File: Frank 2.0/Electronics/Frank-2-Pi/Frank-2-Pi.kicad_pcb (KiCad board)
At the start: 2 copper layers, 11 parts, among them J2 Left motor, J3 Right motor, Q1 DMN6075S, Q2 DMN6075S, U1 adafruit-2448

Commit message: Frank 2.0 electronics WIP.
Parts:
- added C1: 0.1u, Capacitor_SMD:C_0805_2012Metric, B.Cu at (159.4, 107.0)
- added C10: 100u, Capacitor_Tantalum_SMD:CP_EIA-3216-18_Kemet-A_Pad1.58x1.35mm_HandSolder, B.Cu at (169.5, 98.4)
- added C11: 0.1u, Capacitor_SMD:C_0805_2012Metric, B.Cu at (165.7, 111.5)
- added C12: 0.1u, Capacitor_SMD:C_0805_2012Metric, B.Cu at (132.1, 138.4)
- added C3: 0.1u, Capacitor_SMD:C_0805_2012Metric, B.Cu at (170.8, 120.0)
- added C5: 0.1u, Capacitor_SMD:C_0805_2012Metric, B.Cu at (168.3, 120.0)
- added C6: 0.1u, Capacitor_SMD:C_0805_2012Metric, B.Cu at (181.6, 97.8)
- added C7: 0.1u, Capacitor_SMD:C_0805_2012Metric, B.Cu at (118.7, 144.1)
- added C8: 0.1u, Capacitor_SMD:C_0805_2012Metric, B.Cu at (169.5, 112.1)
- added C9: 10u, Capacitor_Tantalum_SMD:CP_EIA-3216-18_Kemet-A_Pad1.58x1.35mm_HandSolder, B.Cu at (169.5, 103.5)
- added J1: left wheel sensor, Connector_PinHeader_2.54mm:PinHeader_1x04_P2.54mm_Vertical, F.Cu at (174.0, 147.3)
- added J10: USB-to-controller, Connector_USB:USB_Micro-B_Wuerth_629105150521, B.Cu at (152.4, 94.6)
- added J11: power-connector, Connector_PinHeader_2.54mm:PinHeader_1x03_P2.54mm_Vertical, F.Cu at (121.3, 91.4)
- added J12: servo 3, Connector_PinHeader_2.54mm:PinHeader_1x03_P2.54mm_Vertical, F.Cu at (111.8, 113.7)
- added J13: servo 2, Connector_PinHeader_2.54mm:PinHeader_1x03_P2.54mm_Vertical, F.Cu at (111.8, 109.2)
- added J14: servo 1, Connector_PinHeader_2.54mm:PinHeader_1x03_P2.54mm_Vertical, F.Cu at (111.8, 104.8)
- added J15: GPIO, Connector_PinHeader_2.54mm:PinHeader_1x05_P2.54mm_Vertical, F.Cu at (111.8, 118.7)
- added J16: data-connector, Connector_PinHeader_2.54mm:PinHeader_1x04_P2.54mm_Vertical, F.Cu at (160.7, 91.4)
- added J4: right wheel sensor, Connector_PinHeader_2.54mm:PinHeader_1x04_P2.54mm_Vertical, F.Cu at (136.5, 147.3)
- added J5: Analogue inputs, Connector_PinHeader_2.54mm:PinHeader_1x03_P2.54mm_Vertical, F.Cu at (181.6, 131.4)
- added J6: LIDAR, Connector_PinHeader_2.54mm:PinHeader_1x04_P2.54mm_Vertical, F.Cu at (112.4, 147.3)
- added J7: Phototransistor, Connector_PinHeader_2.54mm:PinHeader_1x02_P2.54mm_Vertical, F.Cu at (127.0, 147.3)
- added J8: USB-from-battery, Connector_USB:USB_Micro-B_Wuerth_629105150521, B.Cu at (134.0, 94.6)
- added J9: power switch, Connector_PinHeader_2.54mm:PinHeader_1x02_P2.54mm_Vertical, F.Cu at (144.1, 91.4)
- added JP1: l->a2, Jumper:SolderJumper-2_P1.3mm_Open_RoundedPad1.0x1.5mm, B.Cu at (182.9, 118.1)
- added JP2: r->a3, Jumper:SolderJumper-2_P1.3mm_Open_RoundedPad1.0x1.5mm, B.Cu at (182.9, 122.6)
- added R1: 220R, Resistor_SMD:R_0805_2012Metric, B.Cu at (174.0, 143.2)
- added R10: 33K, Resistor_SMD:R_0805_2012Metric, B.Cu at (162.6, 111.8)
- added R11: 15K, Resistor_SMD:R_0805_2012Metric, B.Cu at (172.7, 108.6)
- added R12: 10K, Resistor_SMD:R_0805_2012Metric, B.Cu at (172.7, 112.4)
- added R13: 15K, Resistor_SMD:R_0805_2012Metric, B.Cu at (182.9, 113.7)
- added R2: 220R, Resistor_SMD:R_0805_2012Metric, B.Cu at (136.5, 143.2)
- added R7: 10K, Resistor_SMD:R_0805_2012Metric, B.Cu at (181.6, 143.2)
- added R8: 10K, Resistor_SMD:R_0805_2012Metric, B.Cu at (144.1, 143.2)
- added R9: 6K8, Resistor_SMD:R_0805_2012Metric, B.Cu at (162.6, 107.3)
- added U2: LM2903, Package_SO:Diodes_SO-8EP, B.Cu at (151.1, 108.6)
- added U3: adafruit-1015, reprapltd-kicad:adafruit-1015, F.Cu at (178.4, 108.0)
- added U4: AP1117-33, Package_TO_SOT_SMD:SOT-223-3_TabPin2, B.Cu at (161.9, 101.0)
- added U5: sparkfun-sx1509, reprapltd-kicad:sparkfun-sx1509, F.Cu at (139.7, 131.4)
- C2, C4, Q1, Q2, R3, R4, R5, R6: moved to B.Cu
- moved J2 464.9 mm to (163.2, 147.3), turned to 90 degrees
- moved J3 462.2 mm to (153.0, 147.3), turned to 90 degrees
- moved C4 459.4 mm to (154.3, 144.1)
- moved C2 451.4 mm to (164.5, 144.1)
- moved R5 443.5 mm to (160.7, 129.8), turned to 90 degrees
- moved U1 442.2 mm to (159.4, 133.3), turned to 90 degrees
- moved R6 438.9 mm to (150.5, 129.8), turned to 90 degrees
- moved Q1 431.7 mm to (161.0, 121.0), turned to 270 degrees
- moved R4 430.7 mm to (149.9, 116.5), turned to 90 degrees
- moved Q2 428.9 mm to (150.8, 121.0), turned to 270 degrees
- moved R3 422.5 mm to (160.0, 116.5), turned to 90 degrees
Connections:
- net GPIO16 renamed IO2
- net GPIO6 renamed IO1
- U1 pad 12: GPIO12 -> IO3
- U1 pad 18: GPIO13 -> IO0
- U1 pad 7: Net-(U1-Pad7) -> GND

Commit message: Now with indicator LEDs...
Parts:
- added D1: FLASH, LED_SMD:LED_0805_2012Metric, B.Cu at (115.6, 120.0)
- added D2: 5VLED, LED_SMD:LED_0805_2012Metric, B.Cu at (120.7, 98.4)
- added D3: 3V3LED, LED_SMD:LED_0805_2012Metric, B.Cu at (120.7, 95.9)
- added R14: 220R, Resistor_SMD:R_0805_2012Metric, B.Cu at (120.0, 118.1)
- added R15: 220R, Resistor_SMD:R_0805_2012Metric, B.Cu at (126.4, 95.2)
- added R16: 220R, Resistor_SMD:R_0805_2012Metric, B.Cu at (123.8, 95.2)
- J15: footprint Connector_PinHeader_2.54mm:PinHeader_1x05_P2.54mm_Vertical -> Connector_PinHeader_2.54mm:PinHeader_1x04_P2.54mm_Vertical
- moved J15 4.44 mm to (111.8, 123.2)
- moved U5 1.91 mm to (139.7, 133.3)
- moved C12 1.27 mm to (132.1, 139.7)
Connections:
- J15 pad 4: Net-(J15-Pad4) -> GND
- U5 pad 6: Net-(J15-Pad1) -> Net-(D1-Pad1)
- U5 pad 7: Net-(J15-Pad2) -> Net-(J15-Pad1)
- U5 pad 8: Net-(J15-Pad3) -> Net-(J15-Pad2)
- U5 pad 9: Net-(J15-Pad4) -> Net-(J15-Pad3)
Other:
- board text added: "LEDs are underneath..."

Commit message: Electronics WIP
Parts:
- added C13: 0.1u, Capacitor_SMD:C_0805_2012Metric, B.Cu at (155.6, 95.9)
- added C14: 0.1u, Capacitor_SMD:C_0805_2012Metric, B.Cu at (174.6, 98.4)
- D1, D2, D3: footprint LED_SMD:LED_0805_2012Metric -> LED_THT:LED_D3.0mm; moved to F.Cu
- moved D3 50.0 mm to (170.2, 102.9), turned to 270 degrees
- moved R16 47.8 mm to (169.5, 109.2), turned to 270 degrees
- moved D2 43.4 mm to (163.8, 102.9), turned to 270 degrees
- moved R15 43.0 mm to (167.0, 109.2), turned to 270 degrees
- moved C1 39.5 mm to (170.8, 144.8)
- moved J11 38.7 mm to (160.0, 91.4)
- moved U2 36.3 mm to (148.6, 144.8)
- moved C8 34.9 mm to (181.0, 145.1)
- moved R9 34.9 mm to (174.0, 140.3)
- moved R10 34.9 mm to (174.0, 144.8)
- moved R11 34.9 mm to (184.2, 141.6)
- moved R12 34.9 mm to (184.2, 145.4)
- moved C11 34.9 mm to (177.2, 144.5)
- moved J16 16.5 mm to (177.2, 91.4), turned to 270 degrees
- moved C9 12.9 mm to (158.8, 96.5), turned to 270 degrees
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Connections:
- R3 pad 2: IO2 -> IO1
- R4 pad 2: IO1 -> IO2
- U1 pad 12: IO3 -> IO0
- U1 pad 14: IO2 -> IO1
- U1 pad 16: IO1 -> IO2
- U1 pad 18: IO0 -> IO3
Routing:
- net +5V: track 0.00 -> 57.4 mm, vias 0 -> 2
- net Net-(J10-Pad2): track 0.00 -> 32.5 mm
- net Net-(J8-Pad1): track 0.00 -> 15.8 mm
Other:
- board text removed: "LEDs are underneath..."

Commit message: PCB WIP
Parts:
- added H1: MountingHole, MountingHole:MountingHole_3.2mm_M3, F.Cu at (107.0, 95.0)
- added H2: MountingHole, MountingHole:MountingHole_3.2mm_M3, F.Cu at (107.0, 155.0)
- added H3: MountingHole, MountingHole:MountingHole_3.2mm_M3, F.Cu at (170.0, 95.0)
- added H4: MountingHole, MountingHole:MountingHole_3.2mm_M3, F.Cu at (170.0, 155.0)
- U2: footprint Package_SO:Diodes_SO-8EP -> reprapltd-kicad:Diodes_SO-8EP
- moved J6 65.2 mm to (172.1, 115.7), turned to 0 degrees
- moved C7 52.3 mm to (172.0, 126.7)
- moved R12 50.1 mm to (145.5, 113.5), turned to 180 degrees
- moved C8 49.6 mm to (145.5, 110.4), turned to 180 degrees
- moved J7 45.7 mm to (172.0, 131.6), turned to 0 degrees
- moved R11 44.7 mm to (149.4, 113.5), turned to 180 degrees
- moved C6 42.7 mm to (140.7, 110.0), turned to 0 degrees
- moved C14 41.2 mm to (134.6, 108.2)
- moved C9 41.0 mm to (118.6, 104.8)
- moved U4 41.0 mm to (125.0, 105.4)
- moved C10 41.0 mm to (131.3, 106.7)
- moved J9 37.8 mm to (105.4, 104.4), turned to 180 degrees
- moved J16 33.0 mm to (144.1, 90.8), turned to 90 degrees
- moved U3 27.3 mm to (151.1, 107.3), turned to 90 degrees
- moved C1 27.2 mm to (148.3, 129.5), turned to 0 degrees
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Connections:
- J1 pad 2: IO4 -> IO0
- J4 pad 2: IO6 -> IO2
- R3 pad 2: IO1 -> IO5
- R4 pad 2: IO2 -> IO6
- U1 pad 12: IO0 -> IO4
- U1 pad 14: IO1 -> IO5
- U1 pad 16: IO2 -> IO6
- U1 pad 18: IO3 -> IO7
- U2 pad 1: IO5 -> IO1
- U2 pad 7: IO7 -> IO3
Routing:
- net +3V3: track 0.00 -> 272.3 mm, vias 0 -> 2
- net SCL: track 0.00 -> 81.7 mm
- net SDA: track 0.00 -> 78.7 mm
- net +5V: track 57.4 -> 120.8 mm, vias 2 -> 0
- net INTERRUPT: track 0.00 -> 63.1 mm, vias 0 -> 1
- net IO8: track 0.00 -> 42.8 mm, vias 0 -> 1
- net Net-(J7-Pad2): track 0.00 -> 38.3 mm, vias 0 -> 1
- net Net-(C2-Pad2): track 0.00 -> 35.9 mm
- net IO5: track 0.00 -> 35.3 mm
- net Net-(C2-Pad1): track 0.00 -> 35.2 mm
- net IO0: track 0.00 -> 35.2 mm, vias 0 -> 1
- net IO2: track 0.00 -> 34.7 mm
- net Net-(J10-Pad2): track 32.5 -> 0.02 mm
- net Net-(C4-Pad2): track 0.00 -> 31.5 mm
- net Net-(C4-Pad1): track 0.00 -> 31.3 mm
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- added copper zone on B.Cu, net GND
- added copper zone on F.Cu, net GND

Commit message: PCB WIP
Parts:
- moved JP2 59.7 mm to (133.3, 155.2), turned to 0 degrees
- moved JP1 52.5 mm to (148.2, 154.8)
- moved C2 17.5 mm to (161.4, 154.9)
- moved C4 17.5 mm to (154.7, 154.9)
- moved J2 17.5 mm to (160.4, 158.1)
- moved J3 17.5 mm to (153.4, 158.1)
- moved R1 14.0 mm to (137.2, 153.9)
- moved R7 14.0 mm to (144.8, 153.9)
- moved J1 14.0 mm to (137.2, 158.1)
- moved U2 5.14 mm to (147.8, 132.1)
- moved C1 4.32 mm to (150.4, 125.7)
- moved R6 1.77 mm to (145.8, 125.2), turned to 180 degrees
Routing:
- net Net-(J5-Pad3): track 13.9 -> 116.7 mm
- net Net-(J5-Pad2): track 19.8 -> 83.7 mm
- net INTERRUPT: track 63.1 -> 111.9 mm, vias 1 -> 3
- net Net-(J1-Pad4): track 2.57 -> 48.1 mm, vias 0 -> 2
- net SCL: track 81.7 -> 119.1 mm
- net SDA: track 78.7 -> 105.7 mm
- net GND: track 5.21 -> 31.6 mm, vias 0 -> 3
- net Net-(J4-Pad4): track 21.5 -> 47.9 mm, vias 0 -> 2
- net +5V: track 120.8 -> 142.8 mm, vias 0 -> 2
- net Net-(C11-Pad1): track 5.45 -> 19.2 mm
- net IO4: track 28.8 -> 40.5 mm
- net +3V3: track 272.3 -> 283.6 mm
- net IO3: track 13.1 -> 23.6 mm
- net Net-(C2-Pad1): track 35.2 -> 24.7 mm
- net Net-(C2-Pad2): track 35.9 -> 26.5 mm
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
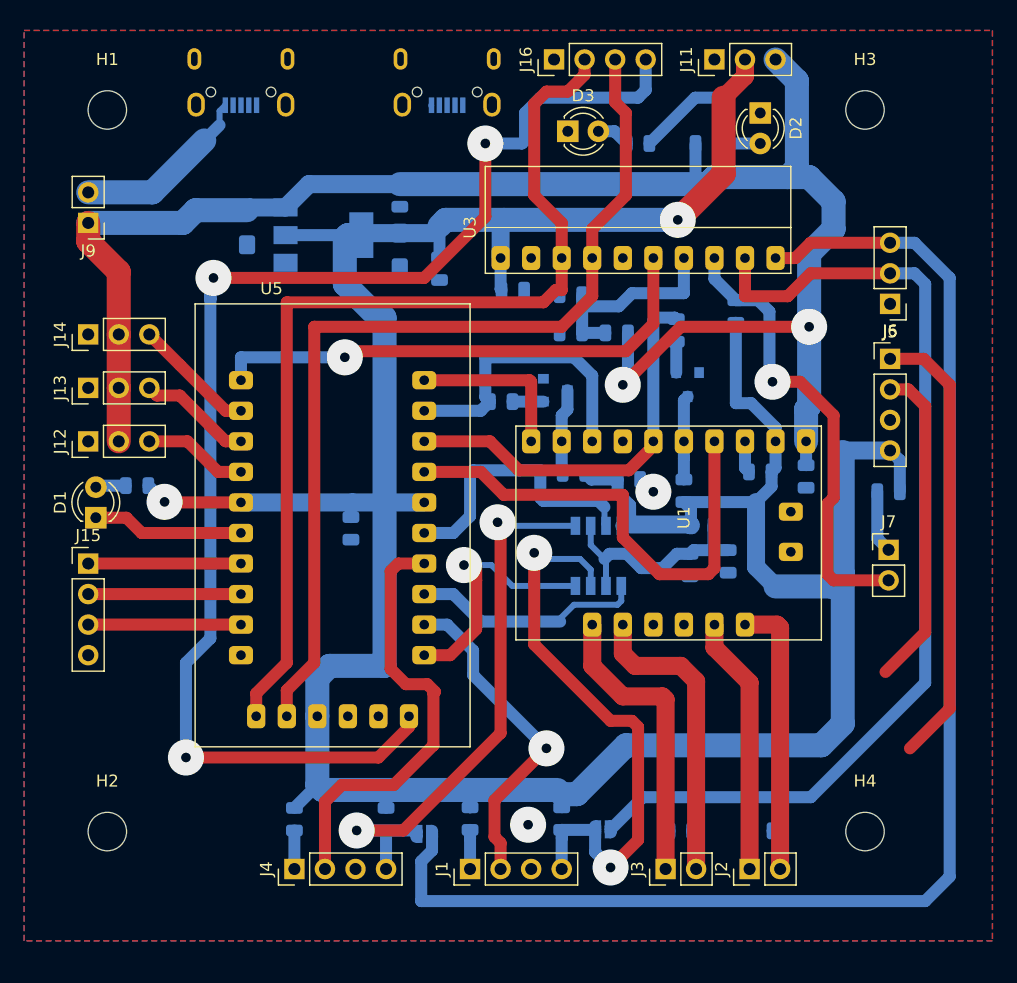
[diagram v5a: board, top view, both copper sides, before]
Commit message: PCB finished (but probably not final...) Except for silks
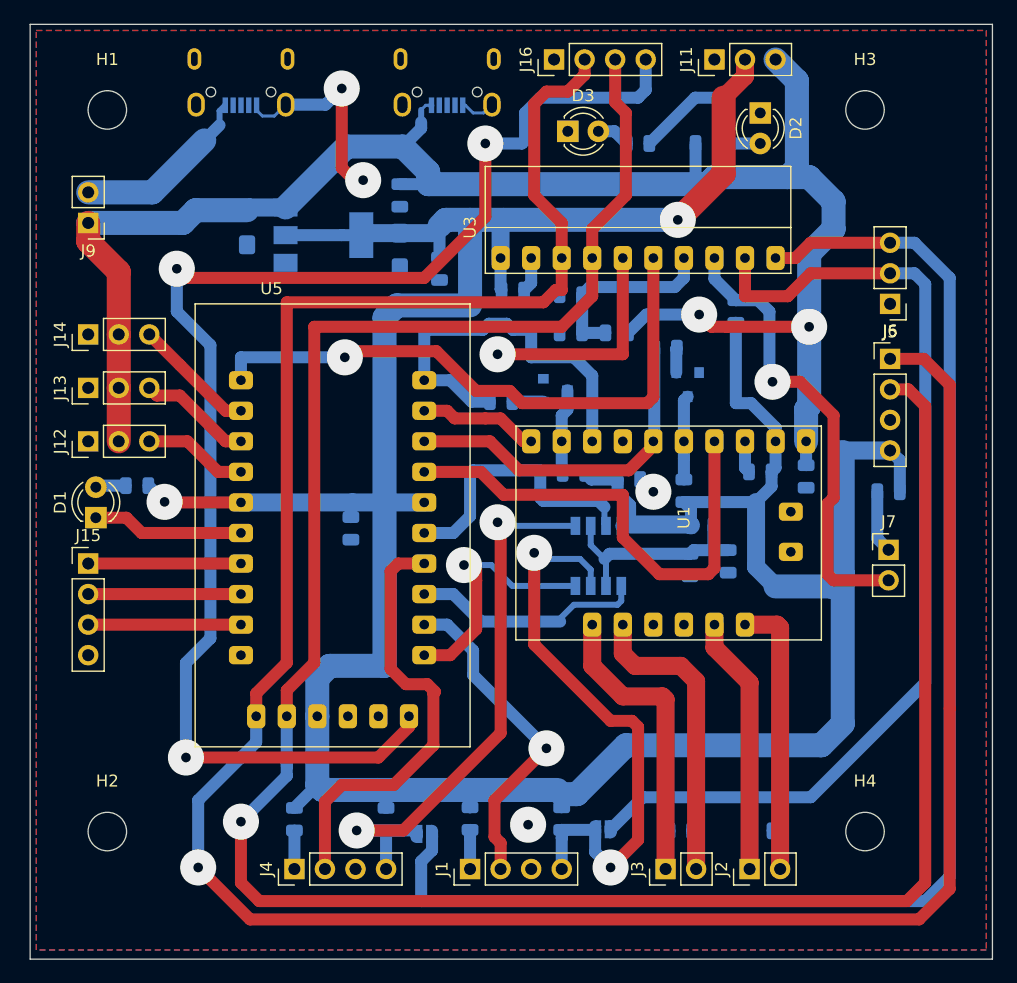
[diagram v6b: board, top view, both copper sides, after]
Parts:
- moved R3 1.72 mm to (153.4, 114.8), turned to 180 degrees
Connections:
- J8 pad 2: Net-(J10-Pad2) -> Net-(J8-Pad2)
- J8 pad 3: Net-(J10-Pad3) -> Net-(J8-Pad3)
- J8 pad 4: Net-(J10-Pad4) -> Net-(J8-Pad4)
- R4 pad 2: IO6 -> IO7
- U1 pad 16: IO6 -> IO7
- U1 pad 18: IO7 -> IO6
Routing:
- net SDA: track 105.7 -> 196.4 mm, vias 0 -> 1
- net SCL: track 119.1 -> 209.3 mm, vias 0 -> 1
- net GND: track 31.6 -> 73.3 mm, vias 3 -> 6
- net IO7: track 13.9 -> 33.2 mm
- net IO6: track 24.6 -> 9.94 mm
- net +5V: track 142.8 -> 150.1 mm
- net IO8: track 42.8 -> 50.0 mm
- net +3V3: track 283.6 -> 289.5 mm
- net INTERRUPT: track 111.9 -> 116.3 mm
- net IO5: track 33.4 -> 29.1 mm
- net Net-(C8-Pad1): track 16.9 -> 15.8 mm
- net Net-(C11-Pad1): track 19.2 -> 18.3 mm
- net Net-(Q1-Pad1): track 2.57 -> 2.05 mm
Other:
- board outline added: 80 x 77.7 mm

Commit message: Updating lots of Frank 2.0 stuff...
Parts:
- moved C10 133.2 mm to (31.0, 19.1)
- moved C12 133.2 mm to (26.9, 42.2)
- moved C13 133.2 mm to (31.0, 14.5)
- moved C14 133.2 mm to (34.3, 20.6)
- moved C2 133.2 mm to (61.0, 67.3)
- moved C4 133.2 mm to (54.4, 67.3)
- moved C6 133.2 mm to (40.4, 22.4)
- moved C9 133.2 mm to (18.3, 17.1)
- moved D3 133.2 mm to (45.0, 9.14)
- moved J1 133.2 mm to (36.8, 70.5)
- moved J12 133.2 mm to (5.08, 34.9)
- moved J14 133.2 mm to (5.08, 26.0)
- moved J16 133.2 mm to (43.8, 3.17)
- moved J2 133.2 mm to (60.1, 70.5)
- moved J3 133.2 mm to (53.1, 70.5)
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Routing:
- net Net-(J1-Pad4): track 48.1 -> 41.7 mm, vias 2 -> 1
- net IO4: track 40.5 -> 35.3 mm
- net SDA: track 196.4 -> 197.7 mm, vias 1 -> 0
- net Net-(J4-Pad4): track 47.9 -> 46.6 mm, vias 2 -> 1
- net INTERRUPT: track 116.3 -> 115.1 mm
- net SCL: track 209.3 -> 209.9 mm, vias 1 -> 0

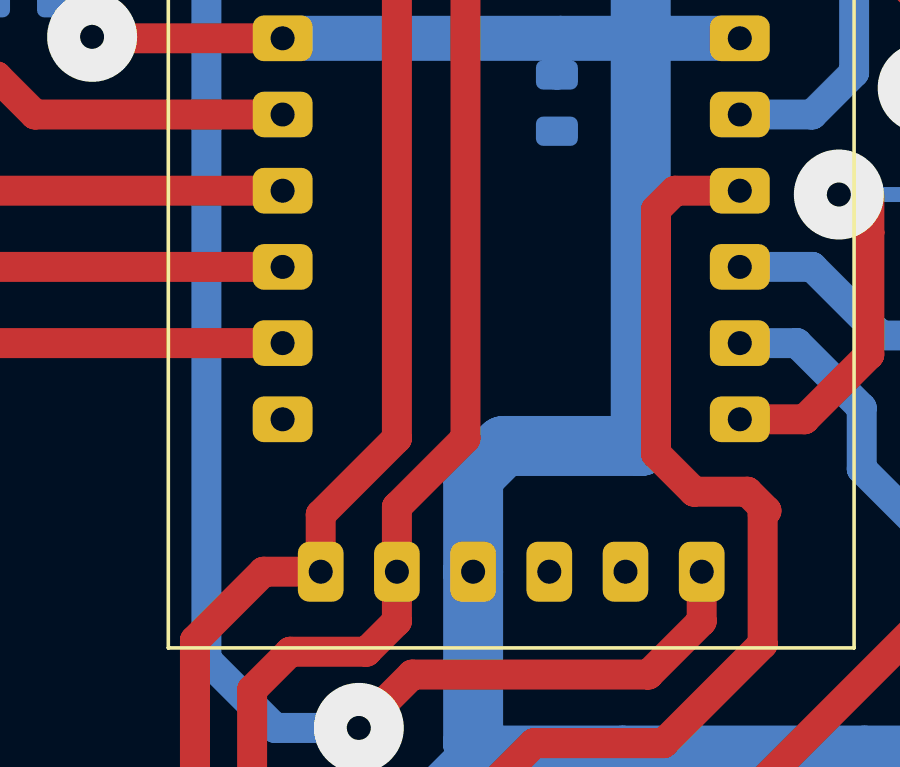
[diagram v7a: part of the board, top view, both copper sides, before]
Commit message: Motor and castor design improvements. I2C pullup resistors added.
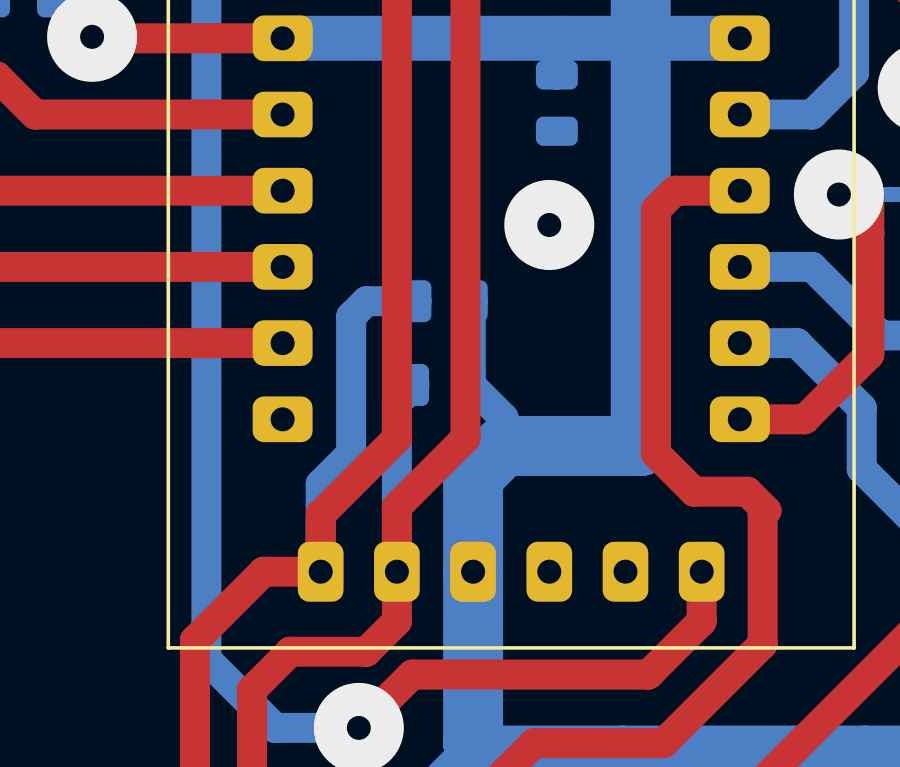
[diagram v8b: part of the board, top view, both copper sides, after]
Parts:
- added R17: 4K7, Resistor_SMD:R_0805_2012Metric, B.Cu at (23.2, 48.8)
- added R18: 4K7, Resistor_SMD:R_0805_2012Metric, B.Cu at (23.1, 51.6)
- R1, R2: value 220R -> 180R
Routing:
- net SCL: track 209.9 -> 221.2 mm
- net SDA: track 197.7 -> 204.2 mm
- net +3V3: track 289.5 -> 294.8 mm
- net GND: vias 6 -> 7
